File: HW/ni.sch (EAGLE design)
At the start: 71 parts, among them IC1 FAN3100TSX, IC2 STM32G071CBU6, IC3 MIC5504-3.3YM5-TR, Q1 FQD12N20L, Q10 CPH3461, Q11 CPH3461, Q12 CPH3461, Q13 BF821SMD, Q14 CPH3461, Q15 BF821SMD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

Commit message: WIFI added
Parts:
- removed D2: S1M, diode:S1M
- removed LS1: CMT-8540S-SMT, CMT-8540S-SMT:CMT-8540S-SMT
- removed Q20: 2n7002k, transistor-small-signal:BSS123
- added C15, C16: (no value), rcl:C-EUC1206
- added C18, C19: (no value), rcl:C-EUC0603
- added IC4: TPS73633DRBR, TPS73633DRBR:TPS73633DRBR
- added J2: (no value), Wurth_Connectors_WR-PHD:6100XX21821_61000821821
- added R17: 10k, rcl:R-EU_R0402
- J3: device EAGLE-BOARD-TO-BOARD_CONNECTORS-rev16c:62100621021 -> OWN_Wurth_Connectors_WR-PHD:OWN_3PIN
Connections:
- removed net LS: IC2.PA2, Q20.G
- removed net N$34: D2.A, LS1.N, Q20.D
- removed net SWO: J3.4
- new net ESP01: IC2.PA1, J2.7
- new net N$1: J2.6, R17.2
- new net VCC: C15.1, C19.1, IC4.NR/FB, IC4.OUT, J2.4, J2.8, R17.1
- net +3V3: no longer J3.1
- net +5V: now also C16.2, C18.2, IC4.EN, IC4.IN; no longer D2.C, LS1.P
- net GN2: now also IC2.PA2; no longer IC2.PA1
- net GND: now also C15.2, C16.1, C18.1, C19.2, IC4.GND, IC4.TAB, J2.1; no longer Q20.S
- net NRST: no longer J3.5
- net SWCLK: now also J3.1; no longer J3.2
- net SWDIO: now also J3.2; no longer J3.6
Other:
- note added: "GN2 new pin!"
- note removed: "TODO: Programmerleiste abändern Montagelöcher Zusätzliche Taster hinzufügen V1.1 change log: 3.3V Versorgung richtig angeschlossen Löcher für Röhren kleiner Bestückungsdruck der Röhren angepasst"

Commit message: ni.brd, ni.sch und 13 weitere dateien aktualisiert...
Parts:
- R1, R10, R4, R7: value 10k -> 15k
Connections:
- net VCC: no longer IC4.NR/FB
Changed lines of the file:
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@@
 <part name="GND22" library="supply1" library_urn="urn:adsk.eagle:library:371" deviceset="GND" device=""/>
 <part name="Q13" library="transistor-pnp" library_urn="urn:adsk.eagle:library:399" deviceset="BF821*" device="SMD" package3d_urn="urn:adsk.eagle:package:28748/2"/>
-<part name="R1" library="rcl" library_urn="urn:adsk.eagle:library:334" deviceset="R-EU_" device="R1206" package3d_urn="urn:adsk.eagle:package:23540/2" value="10k"/>
+<part name="R1" library="rcl" library_urn="urn:adsk.eagle:library:334" deviceset="R-EU_" device="R1206" package3d_urn="urn:adsk.eagle:package:23540/2" value="15k"/>
 <part name="R2" library="rcl" library_urn="urn:adsk.eagle:library:334" deviceset="R-EU_" device="R1206" package3d_urn="urn:adsk.eagle:package:23540/2" value="470k"/>
 <part name="R3" library="rcl" library_urn="urn:adsk.eagle:library:334" deviceset="R-EU_" device="R1206" package3d_urn="urn:adsk.eagle:package:23540/2" value="1M"/>
@@
 <part name="GND23" library="supply1" library_urn="urn:adsk.eagle:library:371" deviceset="GND" device=""/>
 <part name="Q15" library="transistor-pnp" library_urn="urn:adsk.eagle:library:399" deviceset="BF821*" device="SMD" package3d_urn="urn:adsk.eagle:package:28748/2"/>
-<part name="R4" library="rcl" library_urn="urn:adsk.eagle:library:334" deviceset="R-EU_" device="R1206" package3d_urn="urn:adsk.eagle:package:23540/2" value="10k"/>
+<part name="R4" library="rcl" library_urn="urn:adsk.eagle:library:334" deviceset="R-EU_" device="R1206" package3d_urn="urn:adsk.eagle:package:23540/2" value="15k"/>
 <part name="R5" library="rcl" library_urn="urn:adsk.eagle:library:334" deviceset="R-EU_" device="R1206" package3d_urn="urn:adsk.eagle:package:23540/2" value="470k"/>
 <part name="R6" library="rcl" library_urn="urn:adsk.eagle:library:334" deviceset="R-EU_" device="R1206" package3d_urn="urn:adsk.eagle:package:23540/2" value="1M"/>
@@
 <part name="GND31" library="supply1" library_urn="urn:adsk.eagle:library:371" deviceset="GND" device=""/>
 <part name="Q17" library="transistor-pnp" library_urn="urn:adsk.eagle:library:399" deviceset="BF821*" device="SMD" package3d_urn="urn:adsk.eagle:package:28748/2"/>
-<part name="R7" library="rcl" library_urn="urn:adsk.eagle:library:334" deviceset="R-EU_" device="R1206" package3d_urn="urn:adsk.eagle:package:23540/2" value="10k"/>
+<part name="R7" library="rcl" library_urn="urn:adsk.eagle:library:334" deviceset="R-EU_" device="R1206" package3d_urn="urn:adsk.eagle:package:23540/2" value="15k"/>
 <part name="R8" library="rcl" library_urn="urn:adsk.eagle:library:334" deviceset="R-EU_" device="R1206" package3d_urn="urn:adsk.eagle:package:23540/2" value="470k"/>
 <part name="R9" library="rcl" library_urn="urn:adsk.eagle:library:334" deviceset="R-EU_" device="R1206" package3d_urn="urn:adsk.eagle:package:23540/2" value="1M"/>
@@
 <part name="GND32" library="supply1" library_urn="urn:adsk.eagle:library:371" deviceset="GND" device=""/>
 <part name="Q19" library="transistor-pnp" library_urn="urn:adsk.eagle:library:399" deviceset="BF821*" device="SMD" package3d_urn="urn:adsk.eagle:package:28748/2"/>
-<part name="R10" library="rcl" library_urn="urn:adsk.eagle:library:334" deviceset="R-EU_" device="R1206" package3d_urn="urn:adsk.eagle:package:23540/2" value="10k"/>
+<part name="R10" library="rcl" library_urn="urn:adsk.eagle:library:334" deviceset="R-EU_" device="R1206" package3d_urn="urn:adsk.eagle:package:23540/2" value="15k"/>
 <part name="R11" library="rcl" library_urn="urn:adsk.eagle:library:334" deviceset="R-EU_" device="R1206" package3d_urn="urn:adsk.eagle:package:23540/2" value="470k"/>
 <part name="R12" library="rcl" library_urn="urn:adsk.eagle:library:334" deviceset="R-EU_" device="R1206" package3d_urn="urn:adsk.eagle:package:23540/2" value="1M"/>
@@
 <pinref part="P+14" gate="VCC" pin="VCC"/>
 <wire x1="220.98" y1="71.12" x2="220.98" y2="73.66" width="0.1524" layer="91"/>
-<wire x1="220.98" y1="71.12" x2="220.98" y2="66.04" width="0.1524" layer="91"/>
 <junction x="220.98" y="71.12"/>
-<pinref part="IC4" gate="G$1" pin="NR/FB"/>
-<wire x1="220.98" y1="66.04" x2="218.44" y2="66.04" width="0.1524" layer="91"/>
 <pinref part="C15" gate="G$1" pin="1"/>
 <wire x1="226.06" y1="60.96" x2="226.06" y2="71.12" width="0.1524" layer="91"/>

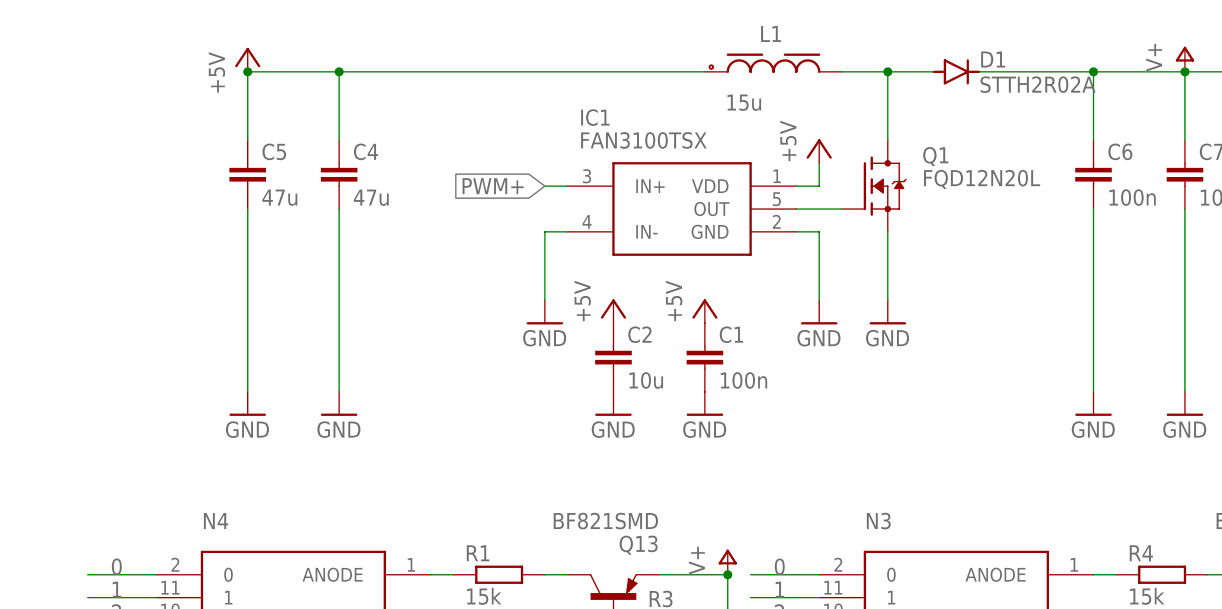
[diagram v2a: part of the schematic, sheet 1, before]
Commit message: working on snubber design
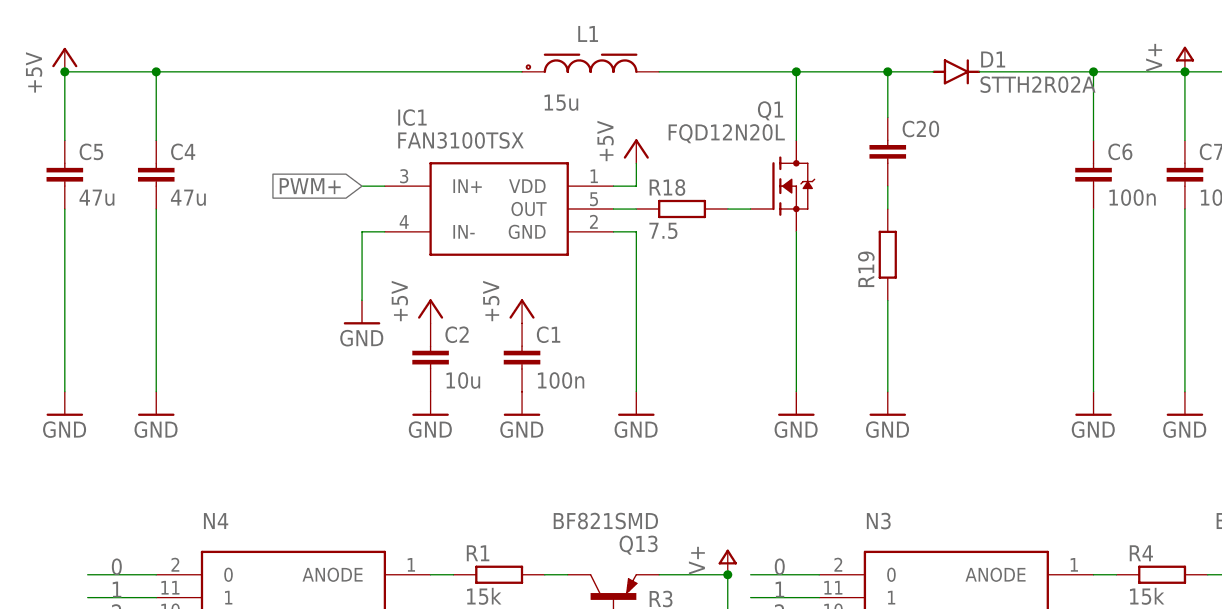
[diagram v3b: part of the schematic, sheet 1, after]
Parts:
- added C20: (no value), rcl:C-EUC0603
- added R18: 7.5, rcl:R-EU_R0603
- added R19: (no value), rcl:R-EU_R0603
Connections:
- new net N$18: IC1.OUT, R18.1
- new net N$25: C20.2, R19.2
- net GND: now also R19.1
- net N$2: now also C20.1
- net N$3: now also R18.2; no longer IC1.OUT
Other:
- moved on the sheet: C1, C2, C4, C5, IC1, L1, Q1

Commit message: rc snubber
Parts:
- C20: device rcl:C-EUC0603 -> rcl:C-EUC1206
- R19: device rcl:R-EU_R0603 -> rcl:R-EU_R1206
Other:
- note added: "Replace with AP2210N-3.3TRG1"
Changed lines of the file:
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@@
 <part name="GND42" library="supply1" library_urn="urn:adsk.eagle:library:371" deviceset="GND" device=""/>
 <part name="R18" library="rcl" library_urn="urn:adsk.eagle:library:334" deviceset="R-EU_" device="R0603" package3d_urn="urn:adsk.eagle:package:23555/3" value="7.5"/>
-<part name="R19" library="rcl" library_urn="urn:adsk.eagle:library:334" deviceset="R-EU_" device="R0603" package3d_urn="urn:adsk.eagle:package:23555/3"/>
-<part name="C20" library="rcl" library_urn="urn:adsk.eagle:library:334" deviceset="C-EU" device="C0603" package3d_urn="urn:adsk.eagle:package:23616/2"/>
+<part name="R19" library="rcl" library_urn="urn:adsk.eagle:library:1468876" deviceset="R-EU_" device="R1206" package3d_urn="urn:adsk.eagle:package:1469523/2"/>
+<part name="C20" library="rcl" library_urn="urn:adsk.eagle:library:1468876" deviceset="C-EU" device="C1206" package3d_urn="urn:adsk.eagle:package:1469291/2"/>
 <part name="GND44" library="supply1" library_urn="urn:adsk.eagle:library:371" deviceset="GND" device=""/>
 </parts>
@@
 </segment>
 </net>
-<net name="N$25" class="0">
+<net name="N$25" class="1">
 <segment>
 <pinref part="C20" gate="G$1" pin="2"/>
@@
 <plain>
 <text x="109.22" y="55.88" size="1.778" layer="94" rot="R90">GN2 new pin!</text>
+<text x="185.42" y="78.74" size="1.778" layer="91">Replace with AP2210N-3.3TRG1
+</text>
+<text x="190.5" y="154.94" size="1.778" layer="91">Replace with AP2210N-3.3TRG1
+</text>
 </plain>
 <instances>
@@
 </drawing>
 <compatibility>
+<note version="6.3" minversion="6.2.2" severity="warning">
+Since Version 6.2.2 text objects can contain more than one line,
+which will not be processed correctly with this version.
+</note>
 <note version="8.2" severity="warning">
 Since Version 8.2, EAGLE supports online libraries. The ids
